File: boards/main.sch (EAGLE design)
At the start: 24 parts, among them T1 PMBT4401,215, T2 PMBT4401,215, U1 MCP1703T-3002E/CB, X1 DF13-4P-1.25V(50), X2 DF13-4P-1.25V(50)

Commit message: Rough schematic, aproximate placement.
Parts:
- removed T1, T2: PMBT4401,215, transistor:MMBT4401LT1-NPN-SOT23-BEC
- removed X1, X2: DF13-4P-1.25V(50), con-molex:53398-04
- added D5: VLMB1300-GS08, SparkFun-LED:LED0603
- added D6: VLMS1300-GS08, SparkFun-LED:LED0603
- added Q1: BC847BS, transistor-small-signal:BC847BS
- added R10, R11: CRCW0603200RFKEA, rcl:R-US_R0603
- added X3, X4: 53398-03, con-molex:53398-03
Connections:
- removed net N$18: R5.1, T1.B
- removed net N$3: R9.1, U$2.OUT
- new net N$11: Q1B.B, R8.1
- new net N$8: D3.C, R6.2
- new net N$9: D4.C, R7.2
- net +3V3: now also D1.A, D2.A, D3.A, D4.A, D5.A, D6.A; no longer R3.2, R4.2, R6.2, R7.2
- net GND: now also Q1A.E, Q1B.E, X3-3.S, X4-3.S; no longer T1.E, T2.E, X1-2.S, X2-2.S
- net LED: now also Q1A.C, R10.1, R3.1, R4.1; no longer D1.C, D2.C, T1.C
- net N$1: now also D1.C, R3.2; no longer D4.A, R7.1
- net N$10: now also D6.C, R11.2; no longer D3.A, R6.1
- net N$2: now also Q1B.C, R11.1, R6.1, R7.1; no longer D3.C, D4.C, T2.C
- net N$4: now also Q1A.B, R5.1; no longer R8.1, T2.B
- net N$6: now also D2.C, R4.2; no longer D2.A, R4.1
- net N$7: now also D5.C, R10.2; no longer D1.A, R3.1
- net RX: now also R9.1, U$2.OUT; no longer X1-3.S, X2-3.S
- net TX: now also X3-2.S, X4-2.S; no longer X1-4.S, X2-4.S
- net VIN: now also X3-1.S, X4-1.S; no longer X1-1.S, X2-1.S
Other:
- moved on the sheet: D1, D2, D3, D4, R3, R4, R5, R6, R7, R8

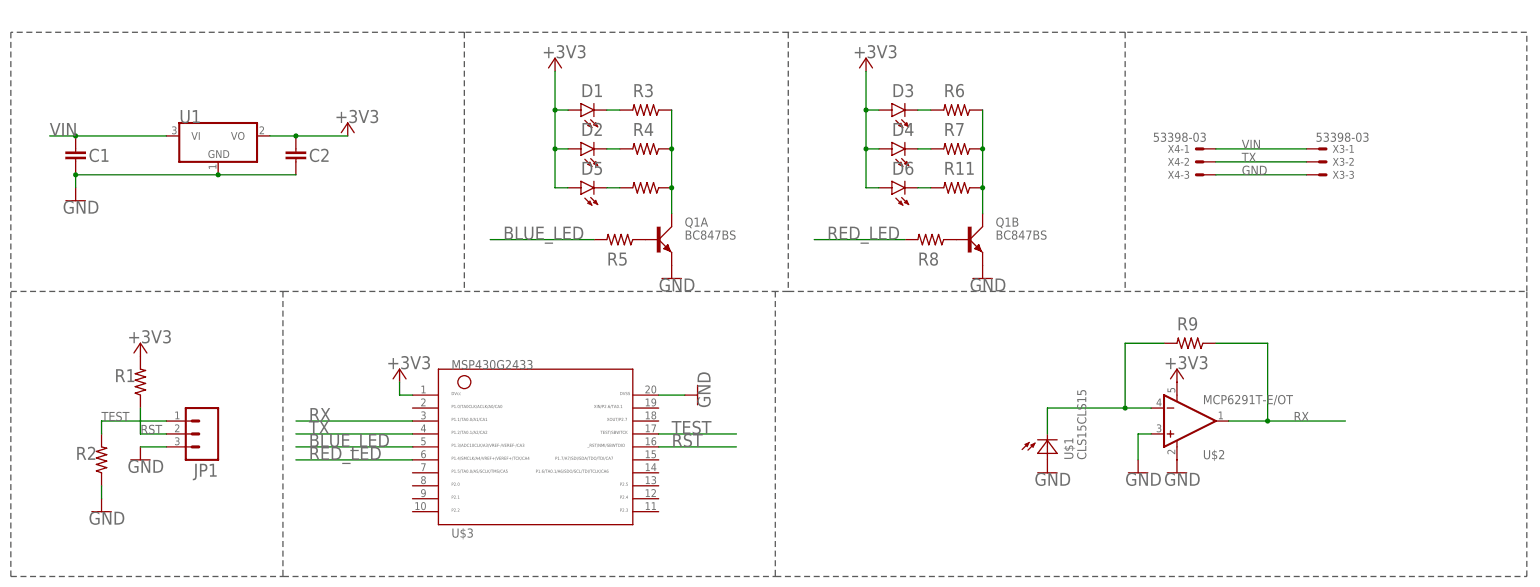
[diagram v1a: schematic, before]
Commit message: Swap msp430 for LPC8* arm processor. Add battery/controller-radio board
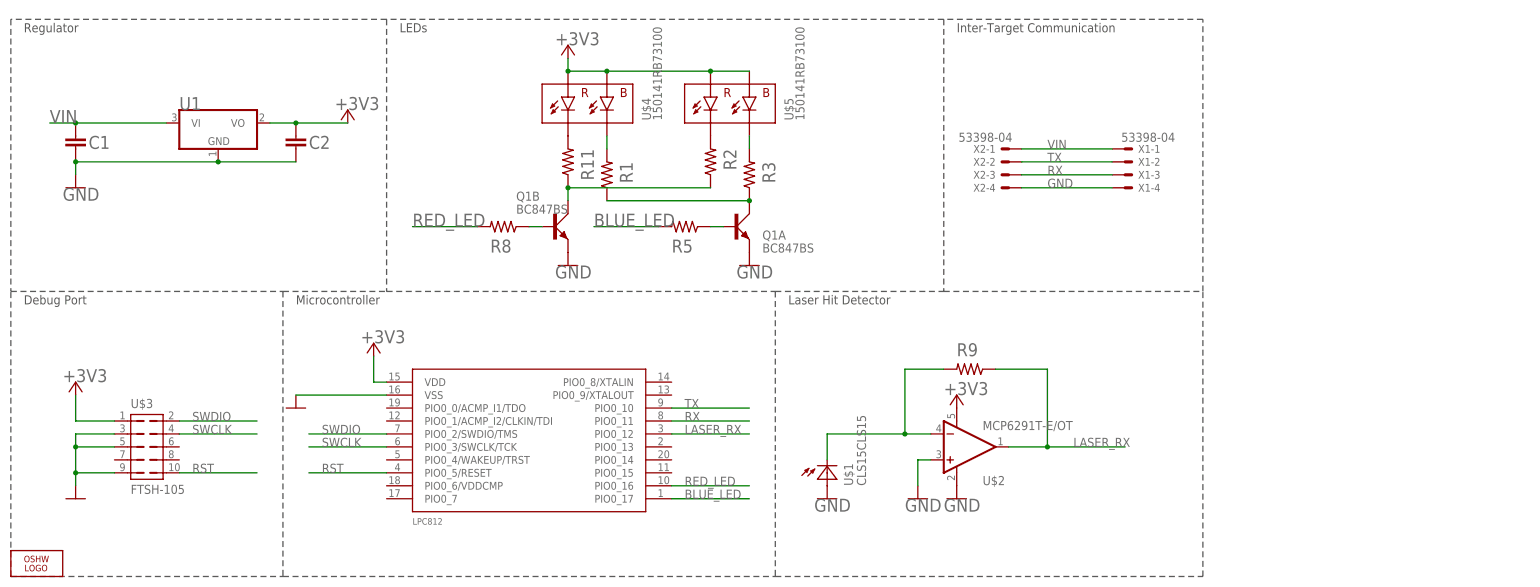
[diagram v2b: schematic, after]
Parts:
- removed D1, D2, D5: VLMB1300-GS08, SparkFun-LED:LED0603
- removed D3, D4, D6: VLMS1300-GS08, SparkFun-LED:LED0603
- removed JP1: (no value), SparkFun-Connectors:M03PTH
- removed R10, R4, R6, R7: CRCW0603200RFKEA, rcl:R-US_R0603
- removed X3, X4: 53398-03, con-molex:53398-03
- added LOGO2: OSHW_LOGO_FILLX0150-NT, ohw-logo:OSHW_LOGO_FILLX0150-NT
- added LPC812: LPC812M101JDH20, LPC800:LPC812M101JDH20
- added U$4, U$5: 150141RB73100, torpedo:LED_RB
- added X1, X2: 53398-04, con-molex:53398-04
- R1, R2: value RK73H1JTTD4702F -> CRCW0603200RFKEA
- U$3: value MSP430G2433 -> FTSH-105; device torpedo:G2X[1/5]2---PW20 -> torpedo:FTSH-105
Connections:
- removed net LED: Q1A.C, R10.1, R3.1, R4.1
- removed net N$10: D6.C, R11.2
- removed net N$9: D4.C, R7.2
- removed net TEST: JP1.1, R2.2, U$3.17
- new net LASER_RX: LPC812.PIO0_12, R9.1, U$2.OUT
- new net N$3: R11.2, U$4.3
- new net SWCLK: LPC812.PIO0_3/SWCLK/TCK, U$3.4
- new net SWDIO: LPC812.PIO0_2/SWDIO/TMS, U$3.2
- net +3V3: now also LPC812.VDD, U$4.1, U$4.2, U$5.1, U$5.2; no longer D1.A, D2.A, D3.A, D4.A, D5.A, D6.A, R1.2
- net BLUE_LED: now also LPC812.PIO0_17; no longer U$3.5
- net GND: now also LPC812.VSS, U$3.3, U$3.5, U$3.9, X1-4.S, X2-4.S; no longer JP1.3, R2.1, U$3.20, X3-3.S, X4-3.S
- net N$1: now also Q1A.C, R1.1, R3.1; no longer D1.C, R3.2
- net N$2: now also R2.1; no longer R6.1, R7.1
- net N$6: now also R2.2, U$5.3; no longer D2.C, R4.2
- net N$7: now also R1.2, U$4.4; no longer D5.C, R10.2
- net N$8: now also R3.2, U$5.4; no longer D3.C, R6.2
- net RED_LED: now also LPC812.PIO0_16; no longer U$3.6
- net RST: now also LPC812.PIO0_5/RESET, U$3.10; no longer JP1.2, R1.1, U$3.16
- net RX: now also LPC812.PIO0_11, X1-3.S, X2-3.S; no longer R9.1, U$2.OUT, U$3.3
- net TX: now also LPC812.PIO0_10, X1-2.S, X2-2.S; no longer U$3.4, X3-2.S, X4-2.S
- net VIN: now also X1-1.S, X2-1.S; no longer X3-1.S, X4-1.S
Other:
- note added: "Debug Port"
- note added: "Inter-Target Communication"
- note added: "LEDs"
- note added: "Laser Hit Detector"
- note added: "Microcontroller"
- note added: "Regulator"
- moved on the sheet: C1, C2, Q1A, Q1B, R1, R11, R2, R3, R5, R8, R9, U$1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
